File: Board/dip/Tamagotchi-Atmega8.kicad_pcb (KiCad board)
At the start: 4 copper layers, 39 parts, among them J1 Conn_02x05_Odd_Even, J2 Conn_01x02, J3 Conn_01x04, J4 Conn_01x07, J5 Conn_01x02, Q1 S8050, SW1 SW_Push, U1 AMS1117, U2 ATmega328P-PU, U3 DS1307+, X1 8MHz, X2 32768kHz

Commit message: dip board finished
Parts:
- U1: value AMS1117 -> LM1117-3.3; footprint Package_TO_SOT_SMD:SOT-223-3_TabPin2 -> Package_TO_SOT_THT:TO-220-3_Vertical; moved to F.Cu
- moved U1 4.02 mm to (156.7, 84.6)
- renumbered REF** to R
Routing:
- net VCC: track 160.1 -> 149.5 mm
- net Net-(J2-Pad1): track 6.67 -> 12.5 mm
- net GND: track 163.3 -> 164.7 mm, vias 0 -> 4
- added copper zone on B.Cu, net GND
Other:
- board outline added: 56.1 x 63.8 mm
- board text added: "+(VCC)"
- board text added: "-"
- board text added: "GND"
- board text added: "KEY"
- board text added: "SCL"
- board text added: "SDA"
- board text added: "SPEAKER"
- board text added: "USBASP"
- board text added: "VBAT"
- board text added: "VCC"
- board text added: "buttons ....."

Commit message: dip board minor fixes, 3D view images, Gerber files
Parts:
- removed the REF** at (173.2, 75.7)
- added REF**: TestPoint_THTPad_D1.5mm_Drill0.7mm, TestPoint:TestPoint_THTPad_D1.5mm_Drill0.7mm, F.Cu at (182.6, 119.4)
- added REF**: TestPoint_THTPad_D1.5mm_Drill0.7mm, TestPoint:TestPoint_THTPad_D1.5mm_Drill0.7mm, F.Cu at (172.2, 75.7)
- added REF**: TestPoint_THTPad_D1.5mm_Drill0.7mm, TestPoint:TestPoint_THTPad_D1.5mm_Drill0.7mm, F.Cu at (194.1, 119.4)
- moved REF** 1.27 mm to (188.2, 106.2)
- moved REF** 1.27 mm to (188.2, 115.6)
- moved C1 1.02 mm to (157.5, 90.4)
- moved J1 1.02 mm to (191.5, 106.2)
- moved LED1 1.02 mm to (183.1, 79.2)
- moved LED2 1.02 mm to (187.7, 79.2)
- moved LED3 1.02 mm to (192.3, 79.2)
- moved Q1 1.02 mm to (162.8, 114.6)
- moved R6 1.02 mm to (178.3, 90.9)
- moved R7 1.02 mm to (178.3, 87.9)
- moved R8 1.02 mm to (178.3, 84.8)
- moved R9 1.02 mm to (178.3, 66.3)
- moved REF** 1.02 mm to (172.2, 83.3)
- moved REF** 1.02 mm to (172.2, 88.4)
- moved REF** 1.02 mm to (184.7, 98.0)
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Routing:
- net GND: track 164.7 -> 214.3 mm
- net VCC: track 149.5 -> 152.0 mm
- net USBASP_NRST: track 70.3 -> 71.2 mm

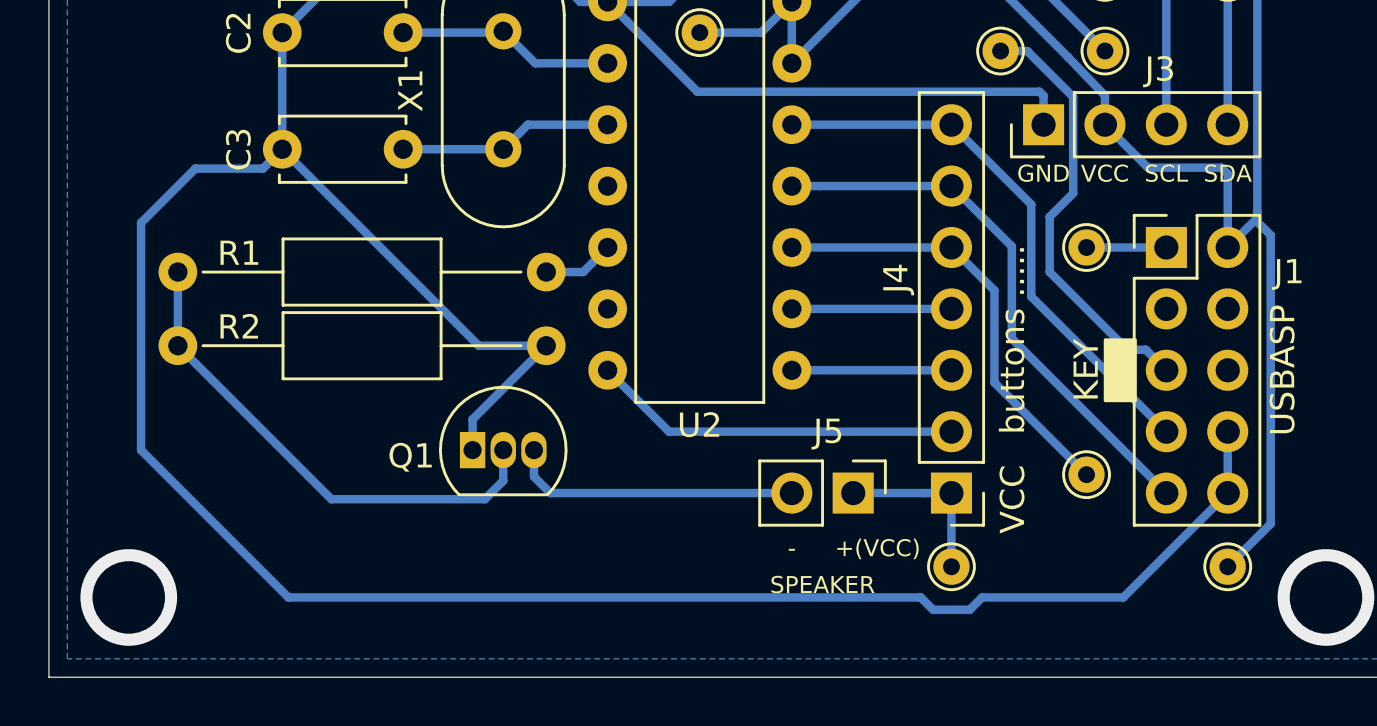
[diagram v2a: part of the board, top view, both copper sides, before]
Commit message: fixed buttons polarity (pull-up state and negative activation)
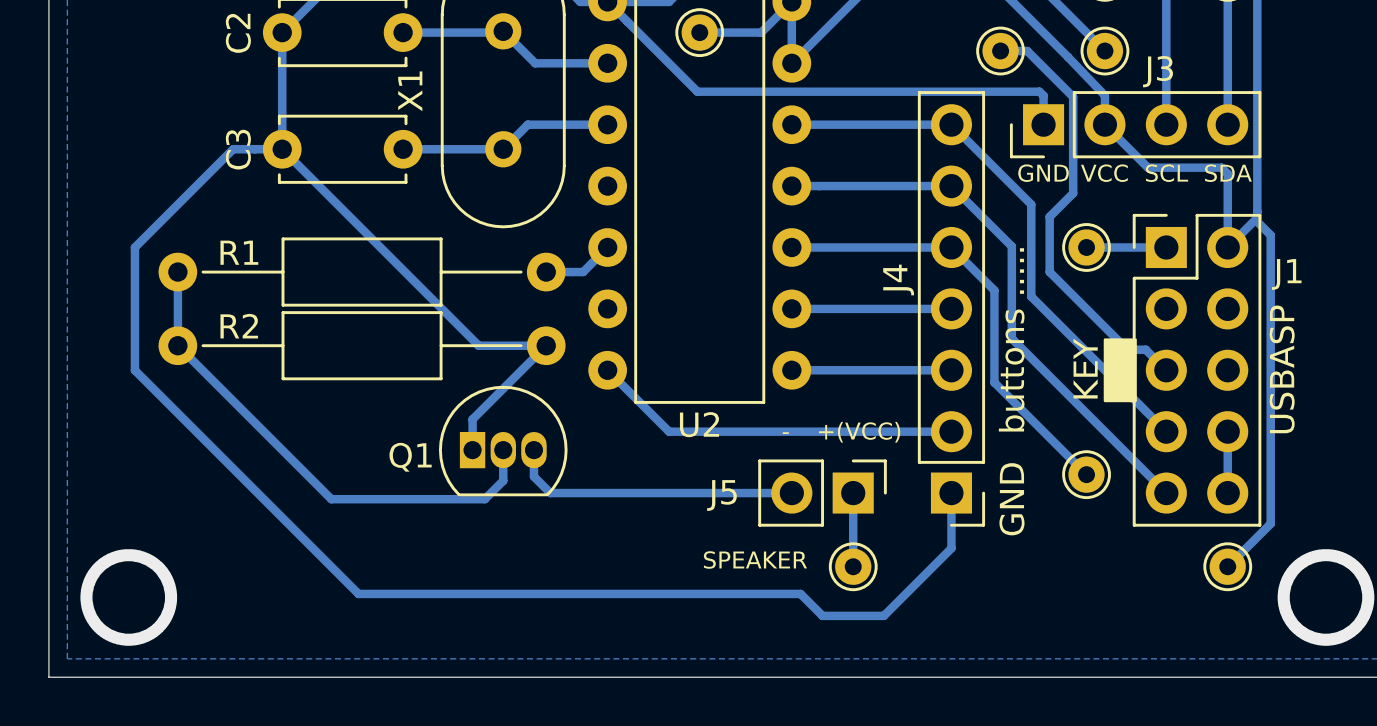
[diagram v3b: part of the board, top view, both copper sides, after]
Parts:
- moved REF** 4.06 mm to (178.6, 119.4)
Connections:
- J4 pad 1: VCC -> GND
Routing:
- net GND: track 214.3 -> 202.4 mm
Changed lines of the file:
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@@
     (thickness 1.6)
     (drawings 18)
-    (tracks 200)
+    (tracks 197)
     (zones 0)
     (modules 41)
@@
   )
   (module TestPoint:TestPoint_THTPad_D1.5mm_Drill0.7mm (layer F.Cu)
-    (at 182.626 119.38)
+    (at 178.562 119.38)
     (descr "THT pad as test Point, diameter 1.5mm, hole diameter 0.7mm")
     (tags "test point THT pad")
@@
     (descr "Through hole straight pin header, 1x02, 2.54mm pitch, single row")
     (tags "Through hole pin header THT 1x02 2.54mm single row")
-    (fp_text reference J5 (at -2.54 1.016) (layer F.SilkS)
+    (fp_text reference J5 (at 0 5.334) (layer F.SilkS)
       (effects (font (size 1 1) (thickness 0.15)))
     )
@@
       (net 17 "Net-(J4-Pad2)"))
     (pad 1 thru_hole rect (at 0 0 180) (size 1.7 1.7) (drill 1) (layers *.Cu *.Mask)
-      (net 2 VCC))
+      (net 1 GND))
     (model ${KISYS3DMOD}/Connector_PinHeader_2.54mm.3dshapes/PinHeader_1x07_P2.54mm_Vertical.wrl
       (at (xyz 0 0 0))
@@
     (effects (font (size 1 1) (thickness 0.2)))
   )
-  (gr_text VCC (at 185.166 116.586 90) (layer F.SilkS)
+  (gr_text GND (at 185.166 116.586 90) (layer F.SilkS)
     (effects (font (size 1 1) (thickness 0.2)))
   )
-  (gr_text - (at 176.022 118.618) (layer F.SilkS)
+  (gr_text - (at 175.768 113.792) (layer F.SilkS)
     (effects (font (size 0.7 0.7) (thickness 0.15)))
   )
-  (gr_text SPEAKER (at 177.292 120.142) (layer F.SilkS)
+  (gr_text SPEAKER (at 174.498 119.126) (layer F.SilkS)
     (effects (font (size 0.7 0.7) (thickness 0.15)))
   )
@@
     (effects (font (size 1 1) (thickness 0.2)))
   )
-  (gr_text "+(VCC)" (at 179.578 118.618) (layer F.SilkS)
+  (gr_text "+(VCC)" (at 178.816 113.792) (layer F.SilkS)
     (effects (font (size 0.7 0.7) (thickness 0.15)))
   )
@@
   (segment (start 156.34863 92.924) (end 155.702 92.27737) (width 0.35) (layer B.Cu) (net 1))
   (segment (start 157.48 92.924) (end 156.34863 92.924) (width 0.35) (layer B.Cu) (net 1))
-  (segment (start 154.140001 102.907999) (end 154.94 102.108) (width 0.35) (layer B.Cu) (net 1))
-  (segment (start 151.346001 102.907999) (end 154.140001 102.907999) (width 0.35) (layer B.Cu) (net 1))
-  (segment (start 194.056 116.332) (end 189.738 120.65) (width 0.35) (layer B.Cu) (net 1))
-  (segment (start 155.194 120.65) (end 149.098 114.554) (width 0.35) (layer B.Cu) (net 1))
-  (segment (start 149.098 114.554) (end 149.098 105.156) (width 0.35) (layer B.Cu) (net 1))
-  (segment (start 149.098 105.156) (end 151.346001 102.907999) (width 0.35) (layer B.Cu) (net 1))
-  (segment (start 183.896 120.65) (end 183.388 121.158) (width 0.35) (layer B.Cu) (net 1))
-  (segment (start 189.738 120.65) (end 183.896 120.65) (width 0.35) (layer B.Cu) (net 1))
-  (segment (start 183.388 121.158) (end 181.864 121.158) (width 0.35) (layer B.Cu) (net 1))
-  (segment (start 181.864 121.158) (end 181.356 120.65) (width 0.35) (layer B.Cu) (net 1))
-  (segment (start 181.356 120.65) (end 155.194 120.65) (width 0.35) (layer B.Cu) (net 1))
   (segment (start 183.134 78.232) (end 183.134 79.248) (width 0.35) (layer B.Cu) (net 1))
   (segment (start 180.594 75.692) (end 183.134 78.232) (width 0.35) (layer B.Cu) (net 1))
   (segment (start 172.212 75.692) (end 180.594 75.692) (width 0.35) (layer In1.Cu) (net 1))
+  (segment (start 153.80863 102.108) (end 154.94 102.108) (width 0.35) (layer B.Cu) (net 1))
+  (segment (start 152.908 102.108) (end 153.80863 102.108) (width 0.35) (layer B.Cu) (net 1))
+  (segment (start 148.844 106.172) (end 152.908 102.108) (width 0.35) (layer B.Cu) (net 1))
+  (segment (start 158.097001 120.505001) (end 148.844 111.252) (width 0.35) (layer B.Cu) (net 1))
+  (segment (start 182.626 118.618) (end 179.832 121.412) (width 0.35) (layer B.Cu) (net 1))
+  (segment (start 177.292 121.412) (end 176.385001 120.505001) (width 0.35) (layer B.Cu) (net 1))
+  (segment (start 148.844 111.252) (end 148.844 106.172) (width 0.35) (layer B.Cu) (net 1))
+  (segment (start 182.626 116.332) (end 182.626 118.618) (width 0.35) (layer B.Cu) (net 1))
+  (segment (start 179.832 121.412) (end 177.292 121.412) (width 0.35) (layer B.Cu) (net 1))
+  (segment (start 176.385001 120.505001) (end 158.097001 120.505001) (width 0.35) (layer B.Cu) (net 1))
   (segment (start 172.212 92.202) (end 172.212 97.282) (width 0.35) (layer In1.Cu) (net 2))
   (segment (start 167.386 92.456) (end 168.402 93.472) (width 0.35) (layer B.Cu) (net 2))
@@
   (segment (start 176.022 98.552) (end 179.002081 95.571919) (width 0.35) (layer B.Cu) (net 2))
   (segment (start 187.452 98.298) (end 188.976 99.889919) (width 0.35) (layer B.Cu) (net 2))
-  (segment (start 181.426 116.332) (end 178.562 116.332) (width 0.35) (layer B.Cu) (net 2))
-  (segment (start 182.626 116.332) (end 181.426 116.332) (width 0.35) (layer B.Cu) (net 2))
   (segment (start 158.242 89.662) (end 157.48 90.424) (width 0.35) (layer B.Cu) (net 2))
   (segment (start 158.242 84.582) (end 158.242 89.662) (width 0.35) (layer B.Cu) (net 2))
@@
   (segment (start 187.452 98.298) (end 184.658 95.504) (width 0.35) (layer B.Cu) (net 2))
   (segment (start 179.002081 95.571919) (end 179.07 95.504) (width 0.35) (layer B.Cu) (net 2))
-  (segment (start 182.626 119.38) (end 194.056 119.38) (width 0.35) (layer In1.Cu) (net 2))
   (segment (start 195.834 105.664) (end 195.834 117.602) (width 0.35) (layer B.Cu) (net 2))
   (segment (start 195.281001 104.946999) (end 195.281001 105.111001) (width 0.35) (layer B.Cu) (net 2))
   (segment (start 195.834 117.602) (end 194.056 119.38) (width 0.35) (layer B.Cu) (net 2))
   (segment (start 195.281001 105.111001) (end 195.834 105.664) (width 0.35) (layer B.Cu) (net 2))
-  (segment (start 182.626 116.332) (end 182.626 119.38) (width 0.35) (layer B.Cu) (net 2))
+  (segment (start 178.562 116.332) (end 178.562 119.38) (width 0.35) (layer B.Cu) (net 2))
+  (segment (start 194.056 119.38) (end 178.562 119.38) (width 0.35) (layer In1.Cu) (net 2))
   (segment (start 164.03 97.282) (end 164.084 97.228) (width 0.35) (layer B.Cu) (net 3))
   (segment (start 159.94 97.282) (end 164.03 97.282) (width 0.35) (layer B.Cu) (net 3))
